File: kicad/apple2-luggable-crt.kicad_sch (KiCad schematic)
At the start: 233 parts, among them J1 VIDEO IN, J401 DEFLECTION YOKE, J402 CRT SOCKET BRD, J501 CRT SOCKET BRD, J801 12V UNREG, K6 Jumper_2_Bridged, K9+ Jumper_2_Bridged, K9- Jumper_2_Bridged, Q201 2SA562Y, Q202 2SC1815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

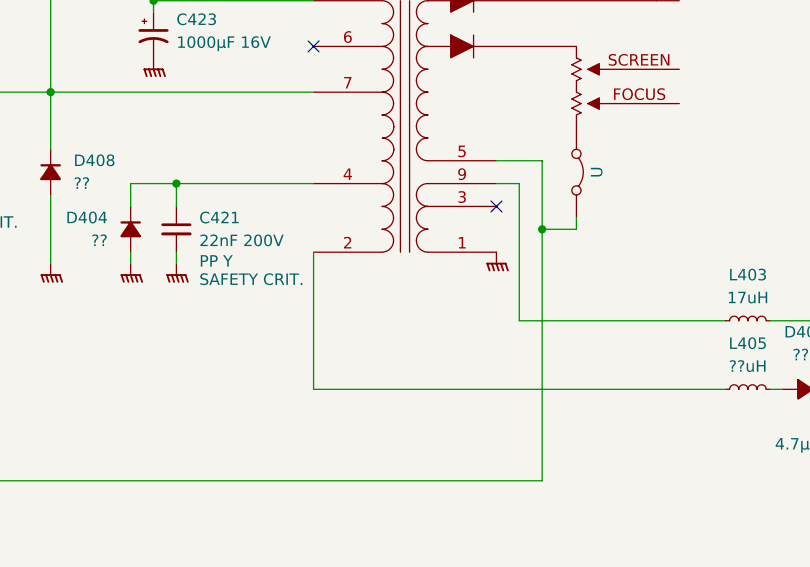
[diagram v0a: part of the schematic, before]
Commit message: add pin 10 to the flyback
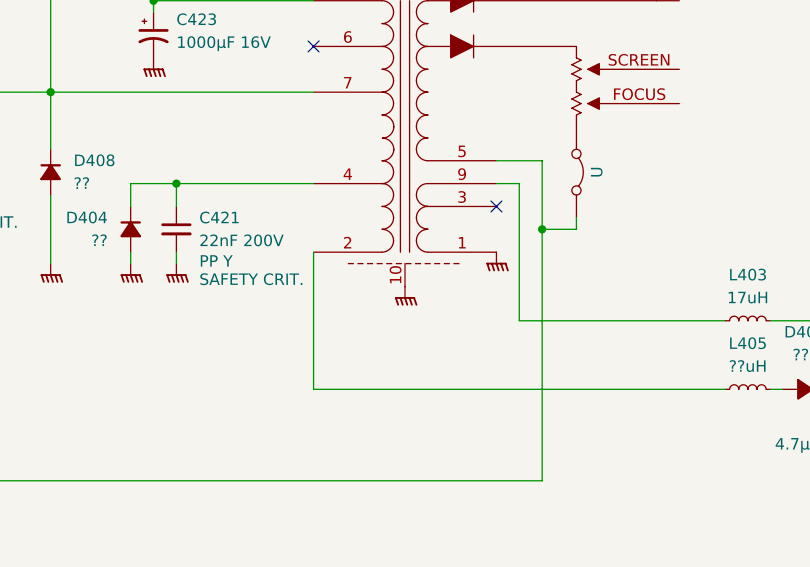
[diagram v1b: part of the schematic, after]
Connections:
- net GNDPWR: now also T451.10
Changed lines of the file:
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@@
 	)
 	(symbol
+		(lib_id "power:GNDPWR")
+		(at 468.63 313.69 0)
+		(mirror y)
+		(unit 1)
+		(exclude_from_sim no)
+		(in_bom yes)
+		(on_board yes)
+		(dnp no)
+		(property "Reference" "#PWR0122"
+			(at 468.63 318.77 0)
+			(effects
+				(font
+					(size 1.27 1.27)
+				)
+				(hide yes)
+			)
+		)
+		(property "Value" "GNDPWR"
+			(at 468.757 317.5 0)
+			(effects
+				(font
+					(size 1.27 1.27)
+				)
+				(hide yes)
+			)
+		)
+		(property "Footprint" ""
+			(at 468.63 314.96 0)
+			(effects
+				(font
+					(size 1.27 1.27)
+				)
+				(hide yes)
+			)
+		)
+		(property "Datasheet" ""
+			(at 468.63 314.96 0)
+			(effects
+				(font
+					(size 1.27 1.27)
+				)
+				(hide yes)
+			)
+		)
+		(property "Description" "Power symbol creates a global label with name \"GNDPWR\" , global ground"
+			(at 468.63 313.69 0)
+			(effects
+				(font
+					(size 1.27 1.27)
+				)
+				(hide yes)
+			)
+		)
+		(pin "1"
+		)
+		(instances
+			(project "apple2-luggable-crt"
+				(path "/b139b959-2b3e-49ad-9a77-d02564fe1a08"
+					(reference "#PWR0122")
+					(unit 1)
+				)
+			)
+		)
+	)
+	(symbol
 		(lib_id "Device:R_Small_US")
 		(at 201.93 96.52 180)
@@
 		(pin "1"
 		)
+		(pin "10"
+		)
 		(instances
